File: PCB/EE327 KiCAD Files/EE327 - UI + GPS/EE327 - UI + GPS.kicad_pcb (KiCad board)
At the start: 4 copper layers, 49.9 x 49.9 mm, 18 parts, among them J1 Conn_01x09_Socket, J2 Conn_01x14_Socket, J3 Conn_01x06_Pin, J4 Conn_01x04_Socket, J5 Conn_01x02_Socket, SW1 SW_Push, SW2 SW_Push, U1 ESP32-WROOM-32E-N4, U3 LDL1117S30R

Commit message: PCB routing started
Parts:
- C1: value C -> 0.1uF; footprint Capacitor_SMD:C_0805_2012Metric -> Capacitor_SMD:C_0805_2012Metric_Pad1.18x1.45mm_HandSolder
- C5, C6: footprint Capacitor_SMD:C_0805_2012Metric -> Capacitor_SMD:C_0805_2012Metric_Pad1.18x1.45mm_HandSolder
- J1: footprint Connector_PinSocket_2.54mm:PinSocket_1x09_P2.54mm_Vertical -> Connector_PinHeader_2.54mm:PinHeader_1x09_P2.54mm_Vertical
- J2: footprint Connector_PinSocket_2.54mm:PinSocket_1x14_P2.54mm_Vertical -> Connector_PinHeader_2.54mm:PinHeader_1x14_P2.54mm_Vertical
- J3: moved to B.Cu
- J5: value Conn_01x02_Socket -> Conn_01x08_Socket; footprint EE327_Symbols:screw terminal -> EE327_Symbols:CONN_B08B-PNDZS-1_JST; moved to B.Cu
- R1, R2: footprint Resistor_SMD:R_0805_2012Metric -> Resistor_SMD:R_0805_2012Metric_Pad1.20x1.40mm_HandSolder
- SW1, SW2: footprint Button_Switch_THT:SW_PUSH_6mm -> EE327_Symbols:pushbutton
- moved J3 47.3 mm to (146.5, 127.0), turned to 0 degrees
- moved SW2 35.1 mm to (131.6, 102.8)
- moved SW1 35.0 mm to (131.5, 94.8)
- moved J1 34.2 mm to (160.8, 86.6)
- moved J5 20.3 mm to (159.3, 122.4), turned to 180 degrees
- moved J4 18.7 mm to (162.5, 114.0), turned to -90 degrees
- moved J2 7.26 mm to (167.8, 86.4)
- moved D4 7.01 mm to (130.0, 122.5)
- moved R5 7.01 mm to (130.0, 117.4)
- moved R2 5.87 mm to (130.3, 113.1)
- moved C5 5.87 mm to (138.1, 119.0)
- moved C6 5.87 mm to (142.2, 107.0)
- moved D1 5.87 mm to (148.4, 113.2)
- moved D2 5.87 mm to (148.4, 118.6)
- moved R1 5.87 mm to (130.1, 108.9)
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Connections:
- J2 pad 8: unconnected-(J2-Pin_8-Pad8) -> +3.3V
- J5 pad 1: GND -> /Terminal_5V
- J5 pad 2: /Terminal_5V -> GND
- U1 pad 10: unconnected-(U1-IO25-Pad10) -> /PMIC_~{INT}
- U1 pad 11: unconnected-(U1-IO26-Pad11) -> /PMIC_STAT1
- U1 pad 12: unconnected-(U1-IO27-Pad12) -> /PMIC_STAT2
- U1 pad 13: unconnected-(U1-IO14-Pad13) -> /PMIC_~{PG}
- U1 pad 15: unconnected-(U1-GND-Pad15) -> GND
- U1 pad 30: unconnected-(U1-IO18-Pad30) -> /TFT_SCK
- U1 pad 31: /TFT_SCK -> unconnected-(U1-IO19-Pad31)
- U1 pad 33: unconnected-(U1-IO21-Pad33) -> /SDA
- U1 pad 36: unconnected-(U1-IO22-Pad36) -> /SCL
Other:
- board size 49.9 x 49.9 mm -> 43.9 x 49.9 mm

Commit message: pcb done?
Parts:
- C1: moved to B.Cu
- moved SW1 30.6 mm to (156.5, 112.5), turned to 90 degrees
- moved R1 26.5 mm to (156.4, 106.0), turned to -90 degrees
- moved D4 24.2 mm to (146.5, 104.8), turned to -90 degrees
- moved R2 21.0 mm to (150.0, 106.2), turned to -90 degrees
- moved SW2 20.9 mm to (150.0, 112.6), turned to 90 degrees
- moved R5 18.6 mm to (146.5, 108.7)
- moved D1 8.58 mm to (151.5, 121.2)
- moved J3 7.85 mm to (154.3, 126.8)
- moved C1 7.71 mm to (142.5, 85.3), turned to 0 degrees
- moved J5 7.31 mm to (166.7, 122.2)
- moved D2 6.69 mm to (151.4, 124.6)
- moved C5 5.21 mm to (143.0, 120.5)
- moved U3 5.21 mm to (142.9, 113.3)
- moved J4 2.92 mm to (162.1, 116.9), turned to 180 degrees
- moved J1 2.56 mm to (162.9, 85.1)
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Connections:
- C6 pad 1: +3V3 -> +3.3V
- R1 pad 2: GND -> /ESP_RST
- R2 pad 2: GND -> /BOOT
- R5 pad 1: +3V3 -> +3.3V
- U3 pad 4: +3V3 -> +3.3V
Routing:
- net +3.3V: track 0.00 -> 115.6 mm, vias 0 -> 5
- net /SDA: track 0.00 -> 65.3 mm
- net /SCL: track 0.00 -> 60.8 mm
- net /PMIC_STAT1: track 0.00 -> 53.7 mm, vias 0 -> 1
- net /PMIC_~{INT}: track 0.00 -> 52.2 mm, vias 0 -> 1
- net /PMIC_~{PG}: track 0.00 -> 47.1 mm, vias 0 -> 1
- net /PMIC_STAT2: track 0.00 -> 46.0 mm, vias 0 -> 1
- net /ESP_RST: track 0.00 -> 36.4 mm, vias 0 -> 1
- net /RX0: track 0.00 -> 28.0 mm
- net /TFT_CS: track 0.00 -> 27.2 mm, vias 0 -> 1
- net /TX0: track 0.00 -> 27.0 mm
- net /TFT_DC: track 0.00 -> 24.8 mm, vias 0 -> 1
- net /TFT_RST: track 0.00 -> 21.9 mm, vias 0 -> 1
- net /TFT_MOSI: track 0.00 -> 18.5 mm
- net /BOOT: track 0.00 -> 16.7 mm, vias 0 -> 1
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- added copper zone on In2.Cu, net GND
- removed copper zone on In2.Cu, net +3.3V
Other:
- board size 43.9 x 49.9 mm -> 34.7 x 49 mm
- board text added: "CycloSense AG/OK/JP 2026 EE 327"
- board text added: "SW2"

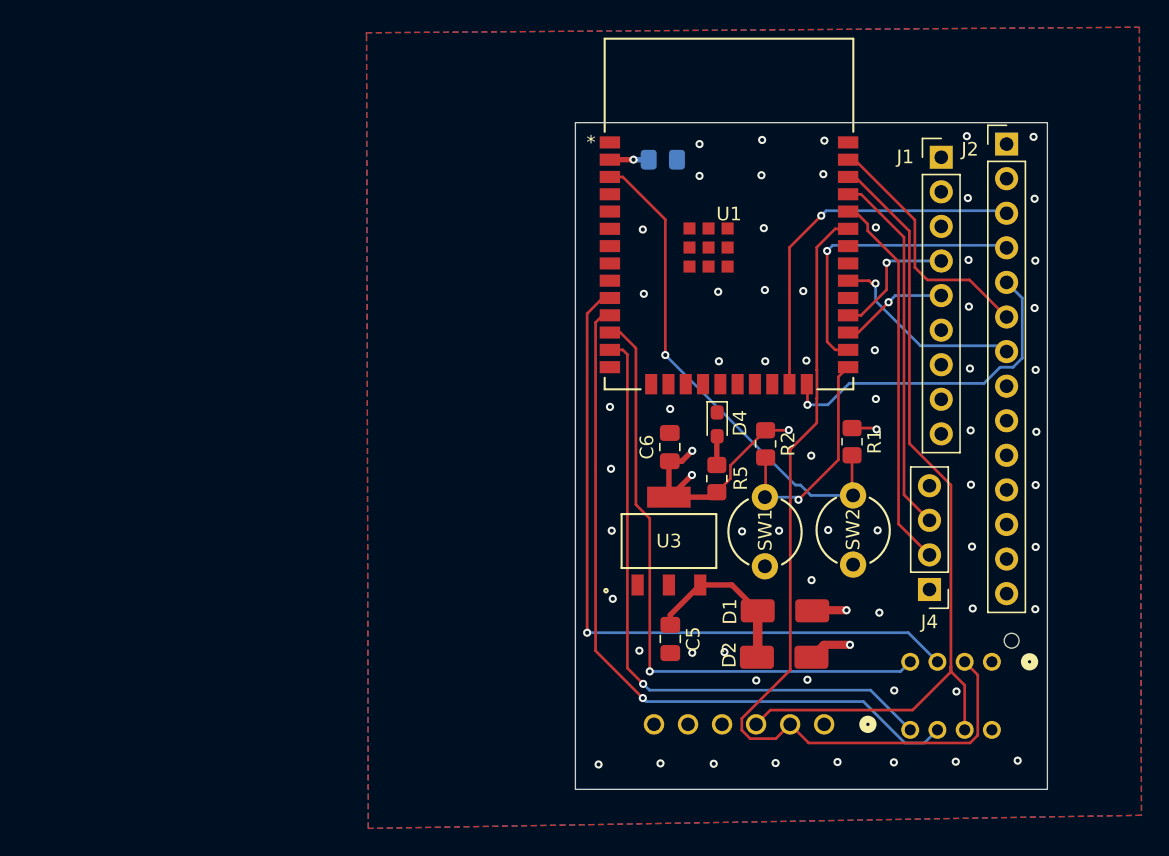
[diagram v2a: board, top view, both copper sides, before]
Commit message: Updated mic connections
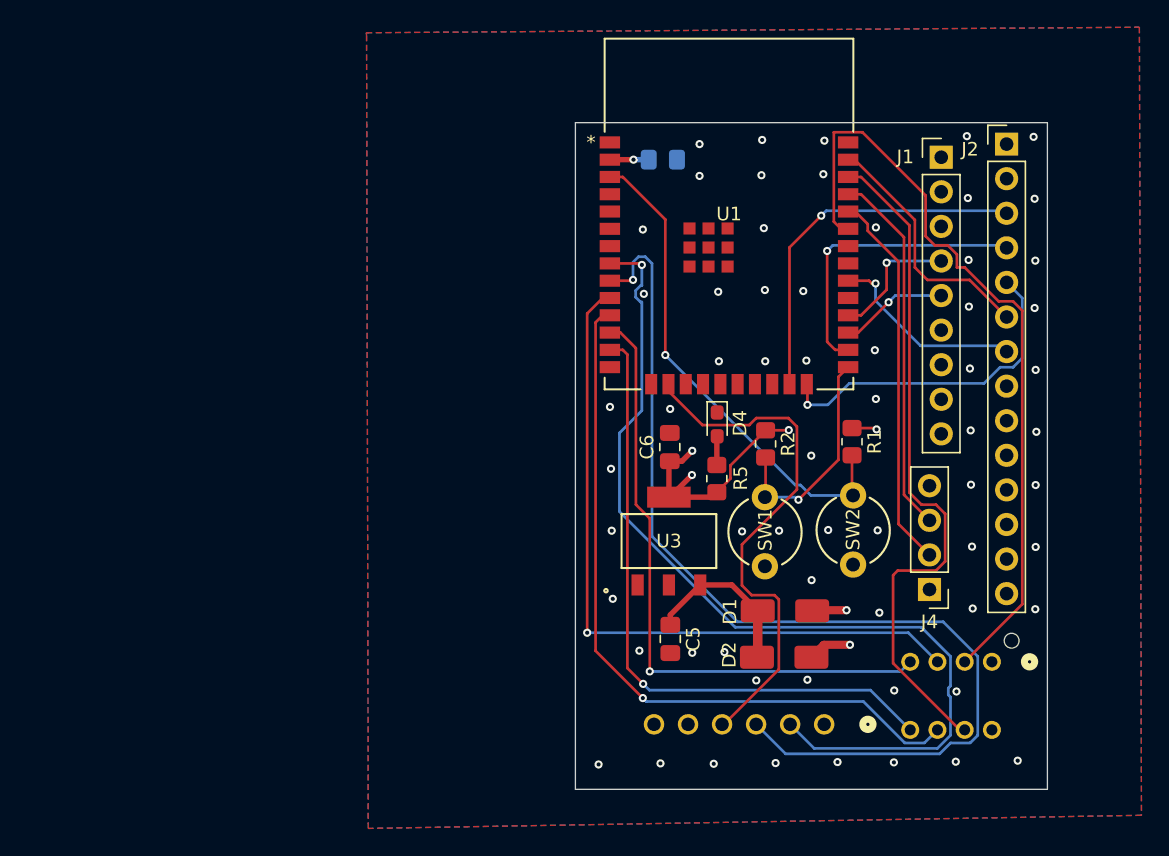
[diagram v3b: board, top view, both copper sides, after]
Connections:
- J3 pad 2: /SDA -> /MIC_SD
- J3 pad 3: /SCL -> /MIC_SCK
- J3 pad 4: /L/R -> /WS
- J3 pad 5: /WS -> GND
- U1 pad 16: unconnected-(U1-IO13-Pad16) -> /WS
- U1 pad 8: unconnected-(U1-IO32-Pad8) -> /MIC_SD
- U1 pad 9: unconnected-(U1-IO33-Pad9) -> /MIC_SCK
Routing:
- net /MIC_SCK: track 0.00 -> 76.0 mm, vias 0 -> 1
- net /MIC_SD: track 0.00 -> 69.3 mm, vias 0 -> 1
- net /WS: track 0.00 -> 38.9 mm
- net /SCL: track 60.8 -> 50.4 mm
- net /SDA: track 65.3 -> 57.0 mm

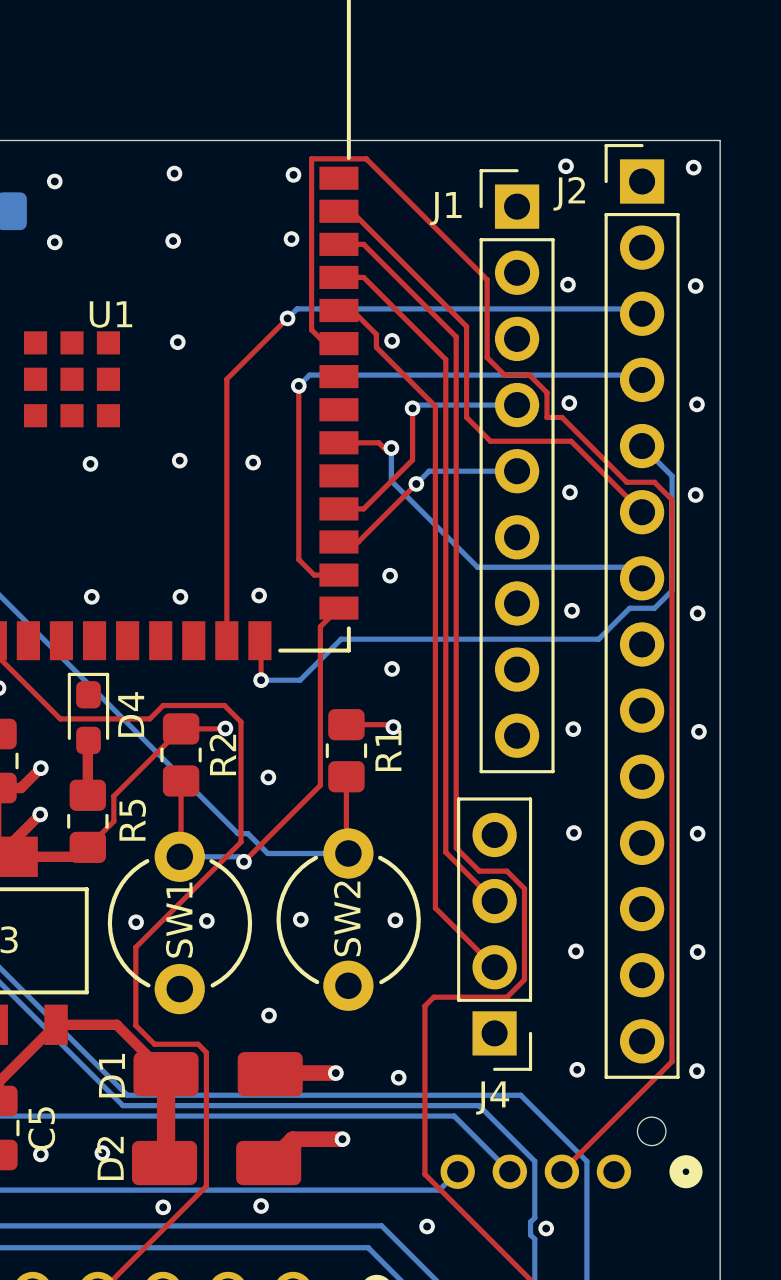
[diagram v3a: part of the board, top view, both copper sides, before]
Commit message: Resolved lingering DRC errors and generated fabrication files
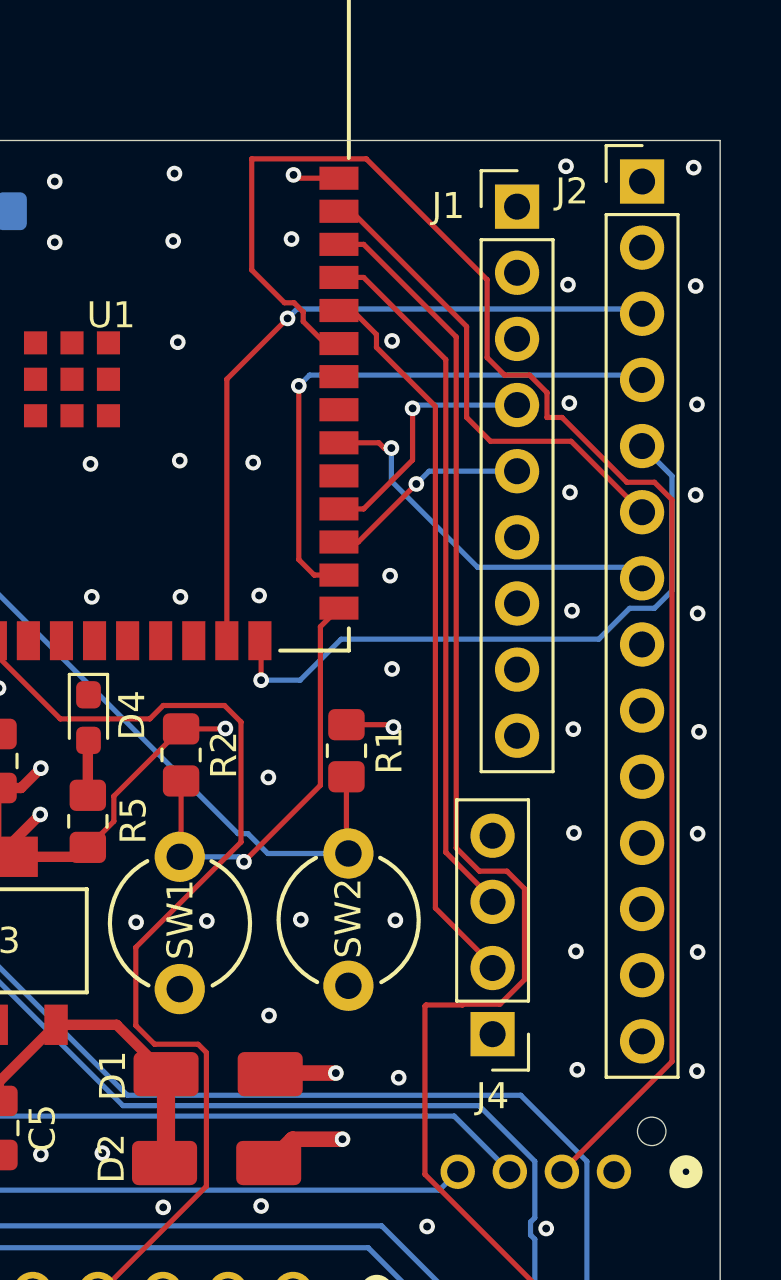
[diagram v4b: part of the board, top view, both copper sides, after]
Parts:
- moved J4 0.08 mm to (162.0, 116.9)
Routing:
- net /SDA: track 57.0 -> 60.4 mm
- net GND: track 0.00 -> 1.80 mm
